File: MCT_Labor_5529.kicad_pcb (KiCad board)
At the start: 2 copper layers, 160 x 100 mm, 142 parts, among them J1 Micro_SD_Card_Det, J10 Conn_01x04_Male, J11 Conn_01x01_Female, J12 Conn_01x01_Female, J13 Conn_01x01_Female, J14 Conn_02x05_Odd_Even, J18 Screw_Terminal_01x02, J2 Conn_02x05_Odd_Even, J3 Grove, J4 Conn_02x04_Odd_Even, J5 Grove, J6 Grove, J7 Conn_01x04_Male, J8 Conn_01x01_Female, Q1 BSS138, SW1 SW_Push, SW2 SW_Push, SW3 SW_SPDT, U1 RC1602A, U10 msp-exp430f5529-LP, U11 MCP73831, U12 TPS73733, U13 TLV61048, U14 LM2776, U2 ULN2003, U3 74148, U4 74_138, U5 NRF24L01_Breakout, U6 74HCT595, U7 ESP-12E, U8 LM75B, U9 STC3100, X1 XBee_S3

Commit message: Kleine Änderungen
Fehler in Kupferflächen und Bestückungsdruck angepasst.
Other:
- board text added: "Arne Alberts, MCT-Labor, 28072020"
- board text removed: "Arne Alberts, MCT-Labor, 27072020"

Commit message: Kleine Anpassungen
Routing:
- net Net-(C17-Pad1): vias 6 -> 4

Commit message: LM75 durch TMP411 ersetzt
-Temperatursensor getauscht
-3,3V 2mm Buchse hinzugeügt
-Bohrlöcher wieder eingefügt
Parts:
- added C28: 100p, Capacitor_SMD:C_0603_1608Metric_Pad1.05x0.95mm_HandSolder, F.Cu at (174.7, 146.4)
- added J15: Conn_01x02, Connector_PinHeader_2.54mm:PinHeader_1x02_P2.54mm_Vertical, F.Cu at (180.9, 147.7)
- added J9: Conn_01x01_Female, HS-Wismar:2mm_Socket, F.Cu at (205.0, 100.0)
- added R1: 10k, Resistor_SMD:R_0603_1608Metric_Pad1.05x0.95mm_HandSolder, F.Cu at (177.5, 139.6)
- added R2: 10k, Resistor_SMD:R_0603_1608Metric_Pad1.05x0.95mm_HandSolder, F.Cu at (177.5, 141.2)
- added R3: 47, Resistor_SMD:R_0603_1608Metric_Pad1.05x0.95mm_HandSolder, F.Cu at (177.2, 147.3)
- added R4: 47, Resistor_SMD:R_0603_1608Metric_Pad1.05x0.95mm_HandSolder, F.Cu at (177.3, 145.6)
- added REF**: MountingHole_3.2mm_M3_Pad_Via, MountingHole:MountingHole_3.2mm_M3_Pad_Via, F.Cu at (206.0, 146.0)
- added REF**: MountingHole_3.2mm_M3_Pad_Via, MountingHole:MountingHole_3.2mm_M3_Pad_Via, F.Cu at (54.0, 54.0)
- added REF**: MountingHole_3.2mm_M3_Pad_Via, MountingHole:MountingHole_3.2mm_M3_Pad_Via, F.Cu at (206.0, 54.0)
- added e: MountingHole_3.2mm_M3_Pad_Via, MountingHole:MountingHole_3.2mm_M3_Pad_Via, F.Cu at (54.0, 146.0)
- U8: value LM75B -> TMP411
- moved R42 9.91 mm to (196.1, 90.6), turned to 90 degrees
- moved J10 8.62 mm to (206.6, 92.3), turned to 180 degrees
- moved C12 6.11 mm to (168.6, 140.6), turned to 270 degrees
- moved D1 5.29 mm to (192.0, 97.5)
- moved U8 4.79 mm to (172.9, 140.3), turned to 90 degrees
- moved J13 0.21 mm to (205.0, 136.0)
- moved J8 0.15 mm to (205.0, 109.0)
- moved J11 0.11 mm to (205.0, 127.0)
- moved J12 0.08 mm to (205.0, 118.0)
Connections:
- C12 pad 1: +3V3 -> GND
- C12 pad 2: GND -> +3V3
- U8 pad 1: /Launchpad/P4.1 -> +3V3
- U8 pad 2: /Launchpad/P4.2 -> Net-(C28-Pad1)
- U8 pad 4: GND -> Net-(R2-Pad2)
- U8 pad 6: GND -> Net-(R1-Pad2)
- U8 pad 7: GND -> /Launchpad/P4.1
- U8 pad 8: +3V3 -> /Launchpad/P4.2
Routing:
- net Net-(C28-Pad1): track 0.00 -> 8.35 mm
- net /Launchpad/P1.6: track 222.9 -> 231.0 mm
- net /Launchpad/P1.5_FAN: track 107.7 -> 114.5 mm
- net Net-(C28-Pad2): track 0.00 -> 5.43 mm
- net GND: track 162.3 -> 157.9 mm, vias 66 -> 65
- net Net-(R1-Pad2): track 0.00 -> 4.35 mm
- net +12V: track 42.7 -> 38.4 mm
- net Net-(J15-Pad2): track 0.00 -> 3.54 mm
- net Net-(J15-Pad1): track 0.00 -> 3.40 mm
- net +3V3: track 74.0 -> 70.7 mm
- net Net-(R2-Pad2): track 0.00 -> 3.09 mm
- net /Launchpad/P4.2: track 194.6 -> 192.1 mm
- net Net-(RN1-Pad3): track 61.4 -> 62.3 mm, vias 2 -> 1
- net Net-(D1-Pad3): track 6.43 -> 7.18 mm
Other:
- board text added: "Arne Alberts, MCT-Labor, 04082020"
- board text removed: "Arne Alberts, MCT-Labor, 28072020"

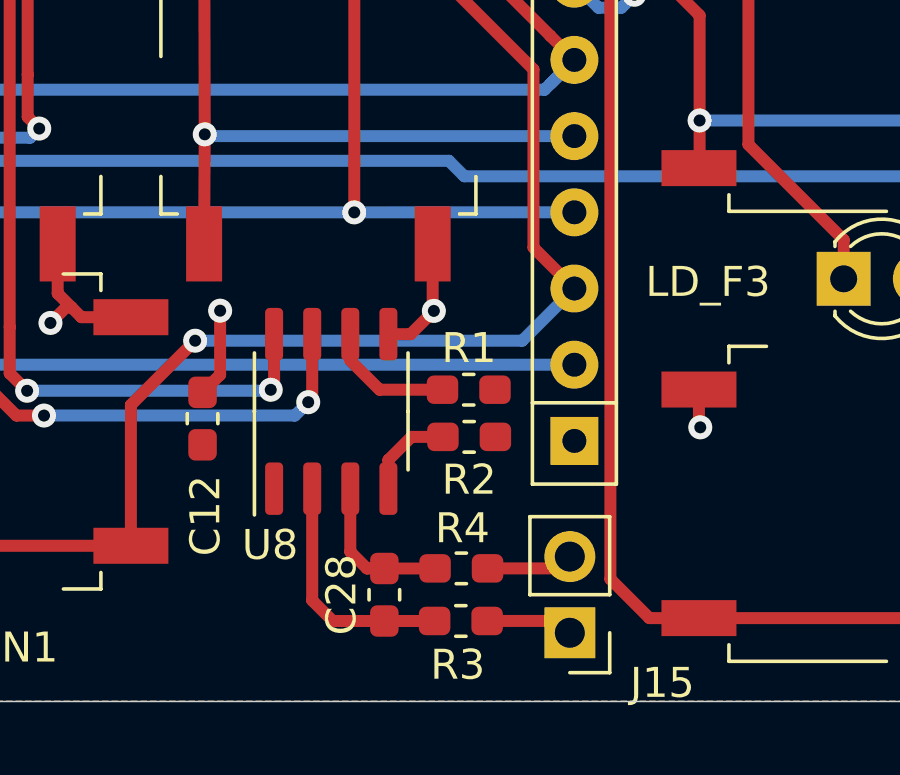
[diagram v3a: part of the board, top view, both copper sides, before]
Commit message: LEDs beim TMP411 hinzugegfügt
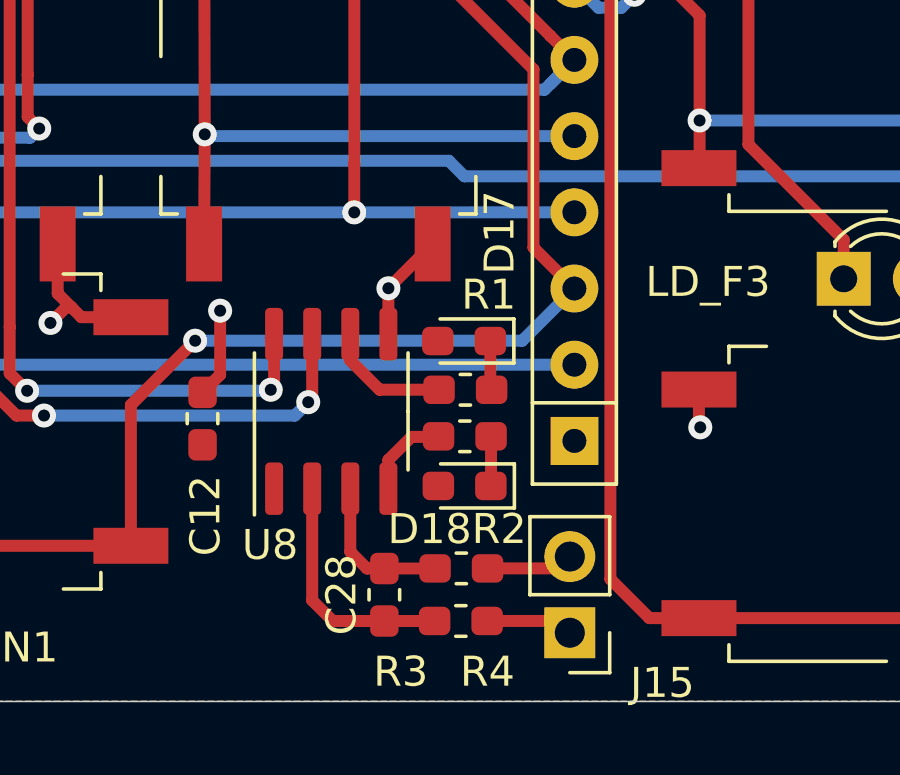
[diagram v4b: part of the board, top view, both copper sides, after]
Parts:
- added D17: LED_Small, LED_SMD:LED_0603_1608Metric_Pad1.05x0.95mm_HandSolder, F.Cu at (177.4, 138.0)
- added D18: LED_Small, LED_SMD:LED_0603_1608Metric_Pad1.05x0.95mm_HandSolder, F.Cu at (177.4, 142.8)
- R1, R2: value 10k -> 220
- moved R2 0.15 mm to (177.4, 141.2)
- moved R1 0.11 mm to (177.4, 139.6)
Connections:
- R1 pad 1: +3V3 -> Net-(D17-Pad1)
- R2 pad 1: +3V3 -> Net-(D18-Pad1)
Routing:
- net Net-(D18-Pad1): track 0.00 -> 1.66 mm
- net Net-(D17-Pad1): track 0.00 -> 1.64 mm

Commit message: minor glitches
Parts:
- removed D10: D_Schottky_Small, Diode_SMD:D_SOD-123
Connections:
- C18 pad 1: +3V3 -> VDC
- D14 pad 1: +3V3 -> VDC
- J18 pad 1: +3V3 -> VDC
- Q1 pad 1: +3V3 -> VDC
- R49 pad 1: +3V3 -> VDC
- U10 pad 16: /Launchpad/~RST -> Net-(U10-Pad16)
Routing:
- net VDC: track 0.00 -> 189.4 mm, vias 0 -> 4
- net /Launchpad/~RST: track 6.34 -> 0.00 mm
- net /Launchpad/P4.1: track 191.9 -> 190.4 mm
- net Net-(R28-Pad2): track 65.5 -> 66.8 mm
- net /Launchpad/P3.3: track 106.4 -> 107.6 mm
- net /Launchpad/P4.2: track 192.1 -> 191.0 mm
- net Net-(C17-Pad1): track 159.1 -> 158.5 mm
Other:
- board text added: "HS-Wismar, FIW/EuI, 04082020"
- board text removed: "Arne Alberts, MCT-Labor, 04082020"

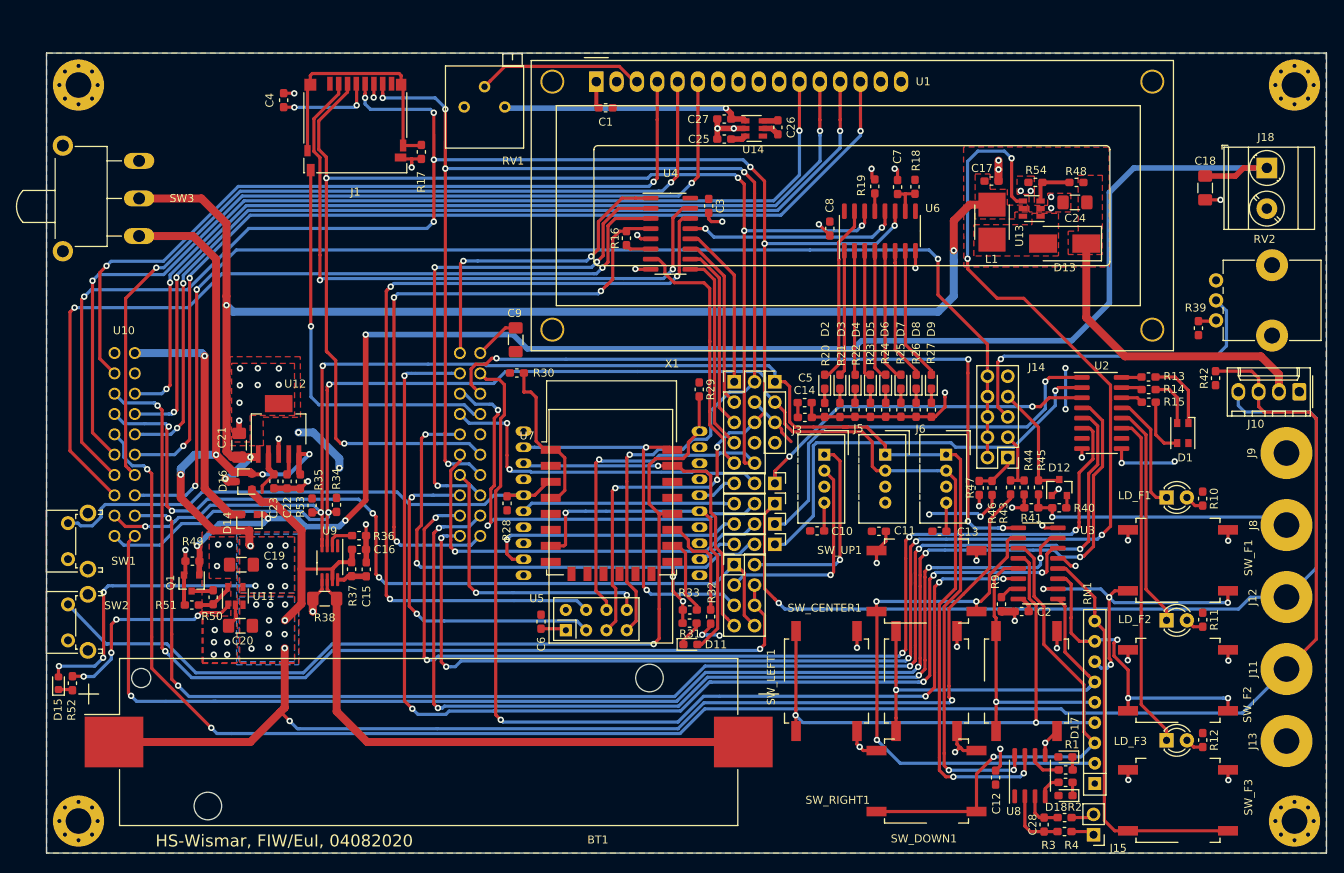
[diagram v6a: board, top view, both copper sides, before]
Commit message: Kupferfläche auf Top -> GND, 3,3V neu gerouted
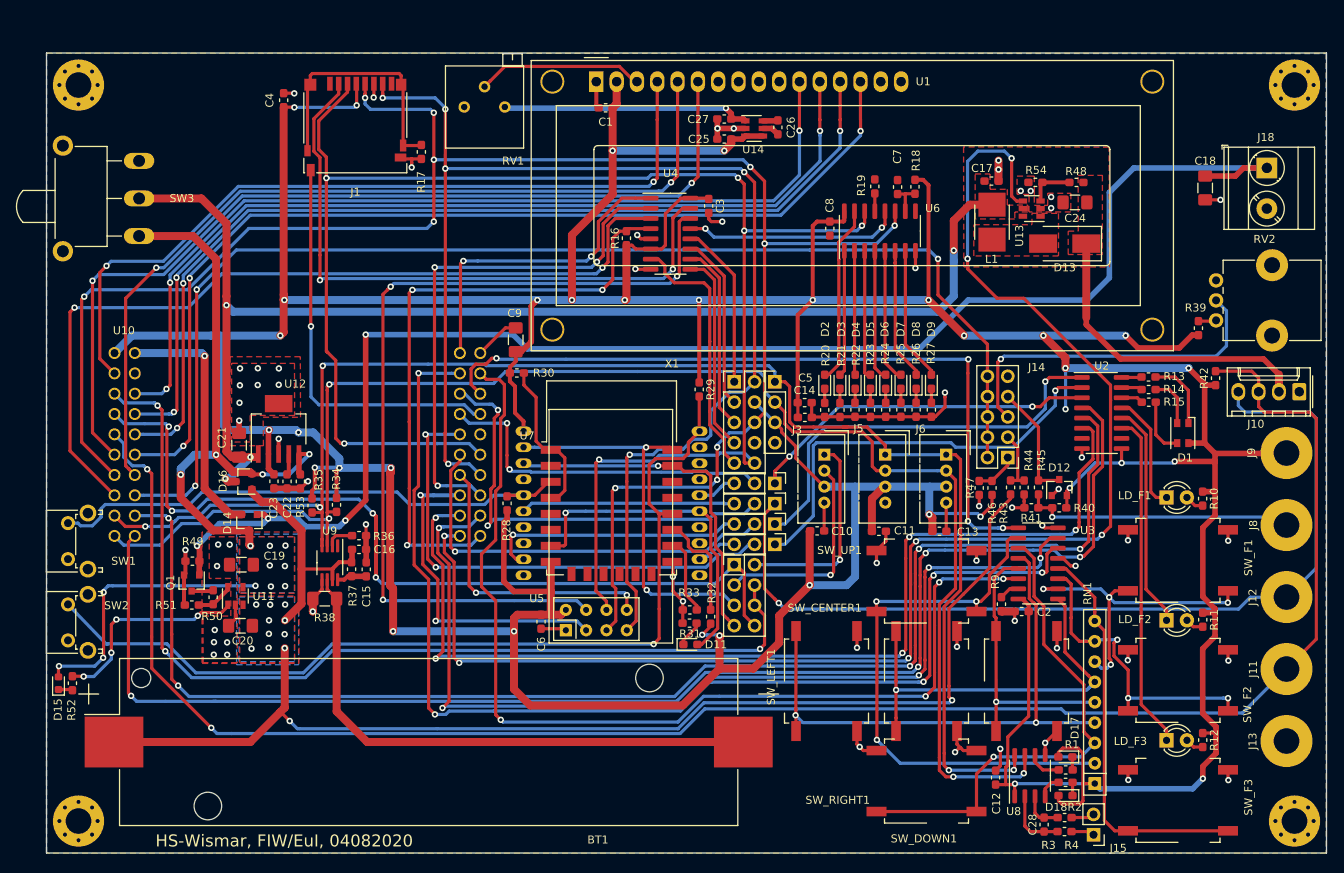
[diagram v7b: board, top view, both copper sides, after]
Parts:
- added G***: LOGO, HS-Wismar:hs-logo_8mm, F.Cu at (197.1, 55.9)
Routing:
- net +3V3: track 70.7 -> 775.3 mm, vias 12 -> 35
- net GND: track 157.4 -> 152.8 mm, vias 65 -> 62
- net /Button_decoder/BTN_S2: track 147.1 -> 144.1 mm
- net /SPI/ADDR_EN: track 80.4 -> 77.8 mm
- net /SPI/NRF_CE: track 43.4 -> 41.1 mm
- net 12V_Enable: track 186.4 -> 184.4 mm
- net Net-(JP3-Pad2): track 64.5 -> 62.5 mm
- net VDC: track 189.4 -> 187.5 mm
- net /Button_decoder/BTN_INT: track 125.8 -> 127.3 mm
- net Net-(U4-Pad14): track 109.4 -> 110.4 mm
- net /LED-Treiber/LED_6: track 132.9 -> 131.9 mm
- net /Launchpad/P3.3: track 107.6 -> 108.2 mm
- net /Launchpad/P1.2_XBEE: track 33.4 -> 32.8 mm
- net +12V: track 38.4 -> 39.0 mm
- net /Launchpad/P4.1: track 190.4 -> 189.9 mm
- removed copper zone on F.Cu, net +3V3

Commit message: Aktuell gefertigte Variante
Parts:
- C15: value 220n -> 100n
- C17, C26: value 1u -> 1µ
- C19, C20: value 4µ7 -> 10µ
- C24: value 10u -> 10µ
- C25, C27: value 2.2u -> 1µ
- D15: footprint LED_SMD:LED_0603_1608Metric -> LED_SMD:LED_0603_1608Metric_Pad1.05x0.95mm_HandSolder
- R10, R11, R12: value 120 -> 220
- R20, R21, R22, R23, R24, R25, R26, R27: value 220 -> 1k
- R45: value 2k2 -> 1k
- R48: value 1.5M -> 680k
- R54: value 107k -> 47k
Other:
- rule trace_min: 0.2 -> 0.25
- rule via_min_size: 0.4 -> 0.6
- board text added: "HS-Wismar, FIW/EuI, 18.01.2021"
- board text removed: "HS-Wismar, FIW/EuI, 04082020"
